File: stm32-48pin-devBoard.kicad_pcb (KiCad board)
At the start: 2 copper layers, 0 parts

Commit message: update USB to longer leads
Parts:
- added C1: 0.1uF, stm32:CAPC2012X100N, F.Cu at (77.4, 87.8)
- added C10: 0.1uF, stm32:CAPC2012X100N, F.Cu at (72.4, 87.8)
- added C11: 18pF, stm32:CAPC2012X100N, F.Cu at (82.6, 87.8)
- added C12: 18pF, stm32:CAPC2012X100N, F.Cu at (87.6, 87.8)
- added C13: 0.1uF, stm32:CAPC2012X100N, F.Cu at (42.2, 90.6)
- added C14: 10uF, stm32:CAPC2012X100N, F.Cu at (47.2, 90.6)
- added C2: 47pF, stm32:CAPC2012X100N, F.Cu at (84.0, 79.6)
- added C3: 47pF, stm32:CAPC2012X100N, F.Cu at (89.0, 79.6)
- added C4: 0.1uF, stm32:CAPC2012X100N, F.Cu at (42.2, 85.0)
- added C5: 0.1uF, stm32:CAPC2012X100N, F.Cu at (47.2, 85.0)
- added C6: 0.1uF, stm32:CAPC2012X100N, F.Cu at (52.4, 85.0)
- added C7: 18pF, stm32:CAPC2012X100N, F.Cu at (57.2, 87.8)
- added C8: 18pF, stm32:CAPC2012X100N, F.Cu at (62.2, 87.8)
- added C9: 0.1uF, stm32:CAPC2012X100N, F.Cu at (67.2, 87.8)
- added D1: LED, stm32:LEDC3216X100N, F.Cu at (74.2, 79.8)
- added J1: USB, stm32:JST_UB-MC5BR3-SD204-4S-NMP, F.Cu at (127.6, 70.8)
- added M1: Mounting Hole, stm32:MTGNP565H328Z565P, F.Cu at (205.4, 53.2)
- added M2: Mounting Hole, stm32:MTGNP565H328Z565P, F.Cu at (208.6, 89.0)
- added M3: Mounting Hole, stm32:MTGNP565H328Z565P, F.Cu at (127.8, 87.2)
- added M4: Mounting Hole, stm32:MTGNP565H328Z565P, F.Cu at (128.6, 53.4)
- added P1: USB-DISCONNECT, stm32:HDRV2W66P254_1X2_508X249X838P, F.Cu at (50.0, 80.0)
- added P2: VBAT, stm32:HDRV2W66P254_1X2_508X249X838P, F.Cu at (42.0, 80.0)
- added P3: VSEL, stm32:HDRV2W66P254_1X2_508X249X838P, F.Cu at (58.2, 80.0)
- added P4: BOOT0, stm32:HDRV2W66P254_1X2_508X249X838P, F.Cu at (90.4, 72.4)
- added P5: JTAG10, stm32:SHDRV10W66P254_2X5_2035X870X609P, F.Cu at (196.8, 79.2)
- added P6: P24, stm32:HDRV24W66P254_1X24_6096X249X838P, F.Cu at (138.4, 52.6)
- added P7: P24, stm32:HDRV24W66P254_1X24_6096X249X838P, F.Cu at (136.8, 88.6)
- added R1: 22R, stm32:RESC2012X100N, F.Cu at (52.2, 87.8)
- added R10: 1k, stm32:RESC2012X100N, F.Cu at (62.4, 85.0)
- added R11: 100R, stm32:RESC2012X100N, F.Cu at (57.4, 85.0)
- added R2: 22R, stm32:RESC2012X100N, F.Cu at (47.2, 87.8)
- added R3: 10k, stm32:RESC2012X100N, F.Cu at (42.2, 87.8)
- added R4: 1.5k, stm32:RESC2012X100N, F.Cu at (79.0, 79.6)
- added R5: 10k, stm32:RESC2012X100N, F.Cu at (87.2, 85.0)
- added R6: 1k, stm32:RESC2012X100N, F.Cu at (82.4, 85.0)
- added R7: 1k, stm32:RESC2012X100N, F.Cu at (77.4, 85.0)
- added R8: 1k, stm32:RESC2012X100N, F.Cu at (72.4, 85.0)
- added R9: 1k, stm32:RESC2012X100N, F.Cu at (67.4, 85.0)
- added S1: RESET, stm32:CKCOMP-PTS525SM10SMTR, F.Cu at (195.0, 58.6)
- added U1: ZXMP2120FFTA, stm32:SOT95P237X112_123-3N, F.Cu at (67.0, 80.4)
- added U2: ZLDO1117, stm32:SOT230P700X180-4N, F.Cu at (56.0, 62.4)
- added U3: STM32-48PIN, stm32:QFP50P900X900X160-48N, F.Cu at (165.0, 71.6)
- added X1: 32kHz, stm32:XTAL8045X200N, F.Cu at (86.8, 61.4)
- added X2: 8MHz, stm32:XTAL8045X200N, F.Cu at (45.4, 73.6)

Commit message: finished pcb
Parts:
- moved R10 132.8 mm to (194.7, 73.8)
- moved R9 127.5 mm to (194.7, 78.8)
- moved R8 123.1 mm to (194.7, 71.3)
- moved C5 122.5 mm to (167.9, 63.8), turned to 45 degrees
- moved C1 119.6 mm to (194.0, 61.0), turned to 90 degrees
- moved C4 118.8 mm to (161.0, 80.4), turned to 270 degrees
- moved R7 117.4 mm to (194.7, 81.3)
- moved R6 112.6 mm to (194.7, 76.3)
- moved X2 112.2 mm to (157.1, 85.1), turned to 180 degrees
- moved C9 108.9 mm to (175.5, 76.0), turned to 315 degrees
- moved C13 106.4 mm to (145.2, 63.8), turned to 90 degrees
- moved C6 105.8 mm to (157.1, 69.8), turned to 135 degrees
- moved P2 105.0 mm to (144.8, 58.4)
- moved C14 99.2 mm to (142.7, 63.8), turned to 90 degrees
- moved R3 92.3 mm to (134.2, 80.8)
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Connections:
- C10 pad 1: +3.3V -> /VBAT
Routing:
- net +3.3V: track 0.00 -> 227.3 mm
- net /PA12: track 0.00 -> 106.6 mm, vias 0 -> 4
- net /PA11: track 0.00 -> 102.6 mm, vias 0 -> 4
- net /nRST: track 0.00 -> 99.3 mm, vias 0 -> 3
- net /PA8: track 0.00 -> 98.3 mm, vias 0 -> 3
- net /JTDO: track 0.00 -> 75.2 mm, vias 0 -> 3
- net /JNTRST: track 0.00 -> 71.5 mm, vias 0 -> 2
- net /JTCK: track 0.00 -> 66.9 mm, vias 0 -> 4
- net /BOOT0: track 0.00 -> 65.9 mm, vias 0 -> 3
- net /PC14: track 0.00 -> 61.1 mm, vias 0 -> 2
- net /PC15: track 0.00 -> 60.7 mm, vias 0 -> 2
- net /JTDI: track 0.00 -> 56.3 mm, vias 0 -> 2
- net +5V: track 0.00 -> 55.1 mm
- net /PB1: track 0.00 -> 52.4 mm, vias 0 -> 2
- net /PB0: track 0.00 -> 52.0 mm, vias 0 -> 2
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- added copper zone on B.Cu, net GND
- added copper zone on F.Cu, net GND
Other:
- board outline added: 83.8 x 48.3 mm
- net class Default: clearance 0.254 -> 0.2032
- rule trace_clearance: 0.254 -> 0.2032

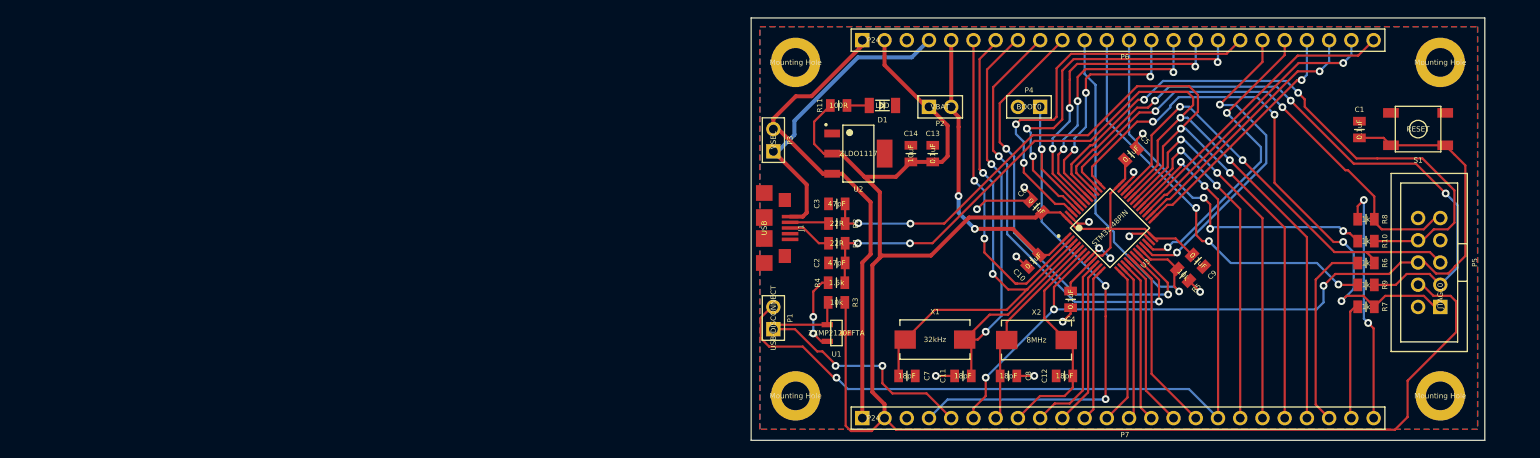
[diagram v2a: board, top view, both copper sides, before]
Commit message: added github label to pcb
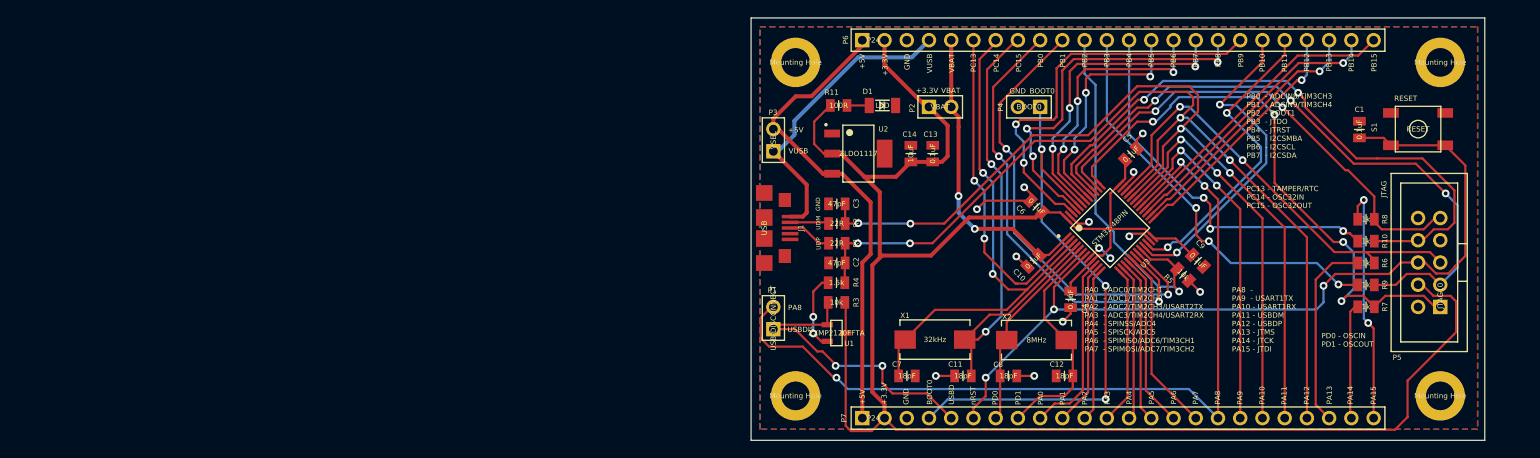
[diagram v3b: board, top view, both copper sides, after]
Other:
- board text added: "+3.3V"
- board text added: "+5V"
- board text added: "BOOT0"
- board text added: "GND"
- board text added: "JTAG"
- board text added: "PA0"
- board text added: "PA0 - ADC0/TIM2CH1 PA1 - ADC1/TIM2CH2 PA2 - ADC2/TIM2CH3/USART2TX PA3 - ADC3/TIM2CH4/USART2RX PA4 - SPINSS/ADC4 PA5 - SPISCK/ADC5 PA6 - SPIMISO/ADC6/TIM3CH1 PA7 - SPIMOSI/ADC7/TIM3CH2"
- board text added: "PA1"
- board text added: "PA10"
- board text added: "PA11"
- board text added: "PA12"
- board text added: "PA13"
- board text added: "PA14"
- board text added: "PA15"
- board text added: "PA2"
- board text added: "PA3"
- board text added: "PA4"
- board text added: "PA5"
- board text added: "PA6"
- board text added: "PA7"
- board text added: "PA8"
- board text added: "PA8 - PA9 - USART1TX PA10 - USART1RX PA11 - USBDM PA12 - USBDP PA13 - JTMS PA14 - JTCK PA15 - JTDI"
- board text added: "PA9"
- board text added: "PB0"
- board text added: "PB0 - ADCIN8/TIM3CH3 PB1 - ADCIN9/TIM3CH4 PB2 - BOOT1 PB3 - JTDO PB4 - JTRST PB5 - I2CSMBA PB6 - I2CSCL PB7 - I2CSDA"
- board text added: "PB1"
- board text added: "PB10"
- board text added: "PB11"
- board text added: "PB12"
- board text added: "PB13"
- board text added: "PB14"
- board text added: "PB15"
- board text added: "PB2"
- board text added: "PB3"
- board text added: "PB4"
- board text added: "PB5"
- board text added: "PB6"
- board text added: "PB7"
- board text added: "PB8"
- board text added: "PB9"
- board text added: "PC13"
- board text added: "PC13 - TAMPER/RTC PC14 - OSC32IN PC15 - OSC32OUT"
- board text added: "PC14"
- board text added: "PC15"
- board text added: "PD0"
- board text added: "PD0 - OSCIN PD1 - OSCOUT"
- board text added: "PD1"
- board text added: "RESET"
- board text added: "UDM"
- board text added: "UDP"
- board text added: "USBD"
- board text added: "USBDIS"
- board text added: "VBAT"
- board text added: "VUSB"
- board text added: "https://github.com/joeferner/stm32-48pin-devBoard"
- board text added: "nRST"

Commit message: version 2013-10-24
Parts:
- moved P5 10.5 mm to (200.7, 71.1), turned to 270 degrees
- moved R7 10.1 mm to (195.0, 71.2)
- moved R8 9.10 mm to (195.0, 80.4)
- moved R9 5.31 mm to (195.0, 73.5)
- moved R10 4.31 mm to (195.0, 78.1)
- moved R6 0.56 mm to (195.0, 75.8)
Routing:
- net GND: track 31.4 -> 60.5 mm, vias 13 -> 19
- net /JTDI: track 56.3 -> 76.8 mm, vias 2 -> 3
- net /JTDO: track 75.2 -> 59.1 mm, vias 3 -> 2
- net /PA14: track 13.3 -> 28.0 mm, vias 0 -> 2
- net /PA15: track 27.9 -> 16.1 mm
- net /JTCK: track 66.9 -> 55.3 mm, vias 4 -> 3
- net /nRST: track 99.3 -> 105.5 mm
- net /PB4: track 43.7 -> 48.2 mm, vias 3 -> 5
- net /JTMS: track 50.9 -> 47.0 mm, vias 2 -> 4
- net +3.3V: track 227.3 -> 229.7 mm
- net /PA13: track 22.0 -> 20.6 mm, vias 0 -> 2
- net /JNTRST: track 71.5 -> 72.8 mm, vias 2 -> 3
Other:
- board text added: "2013-10-24"
